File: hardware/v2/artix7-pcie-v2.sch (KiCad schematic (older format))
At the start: 0 parts

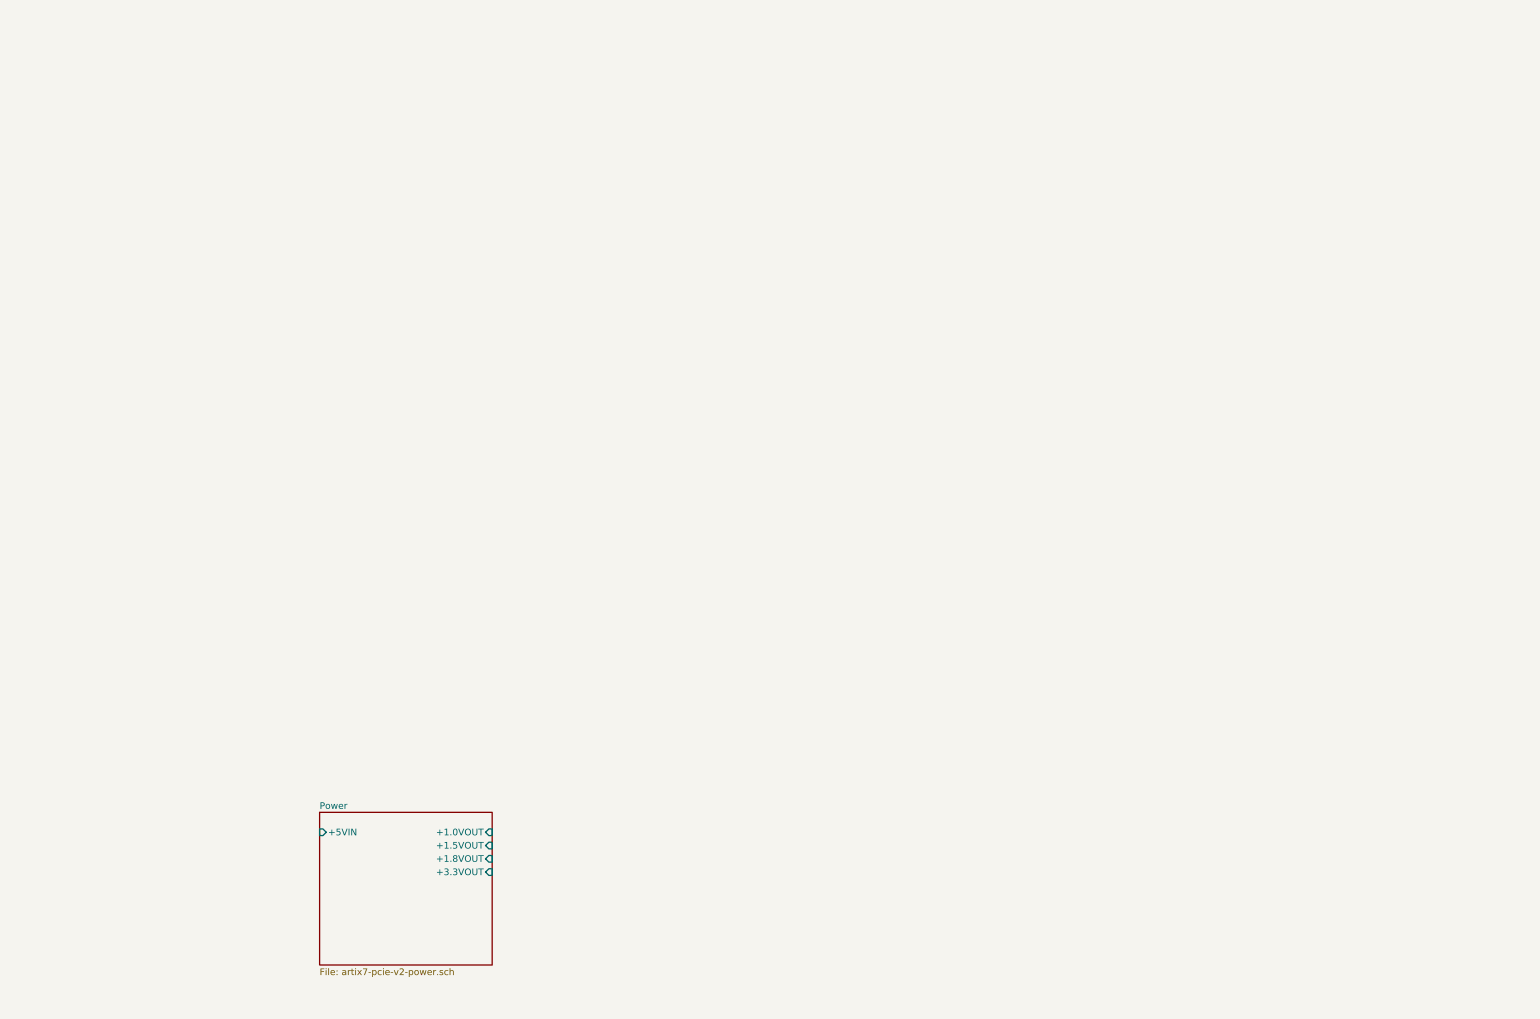
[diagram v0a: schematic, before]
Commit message: v2 schematic : add config block and connectors
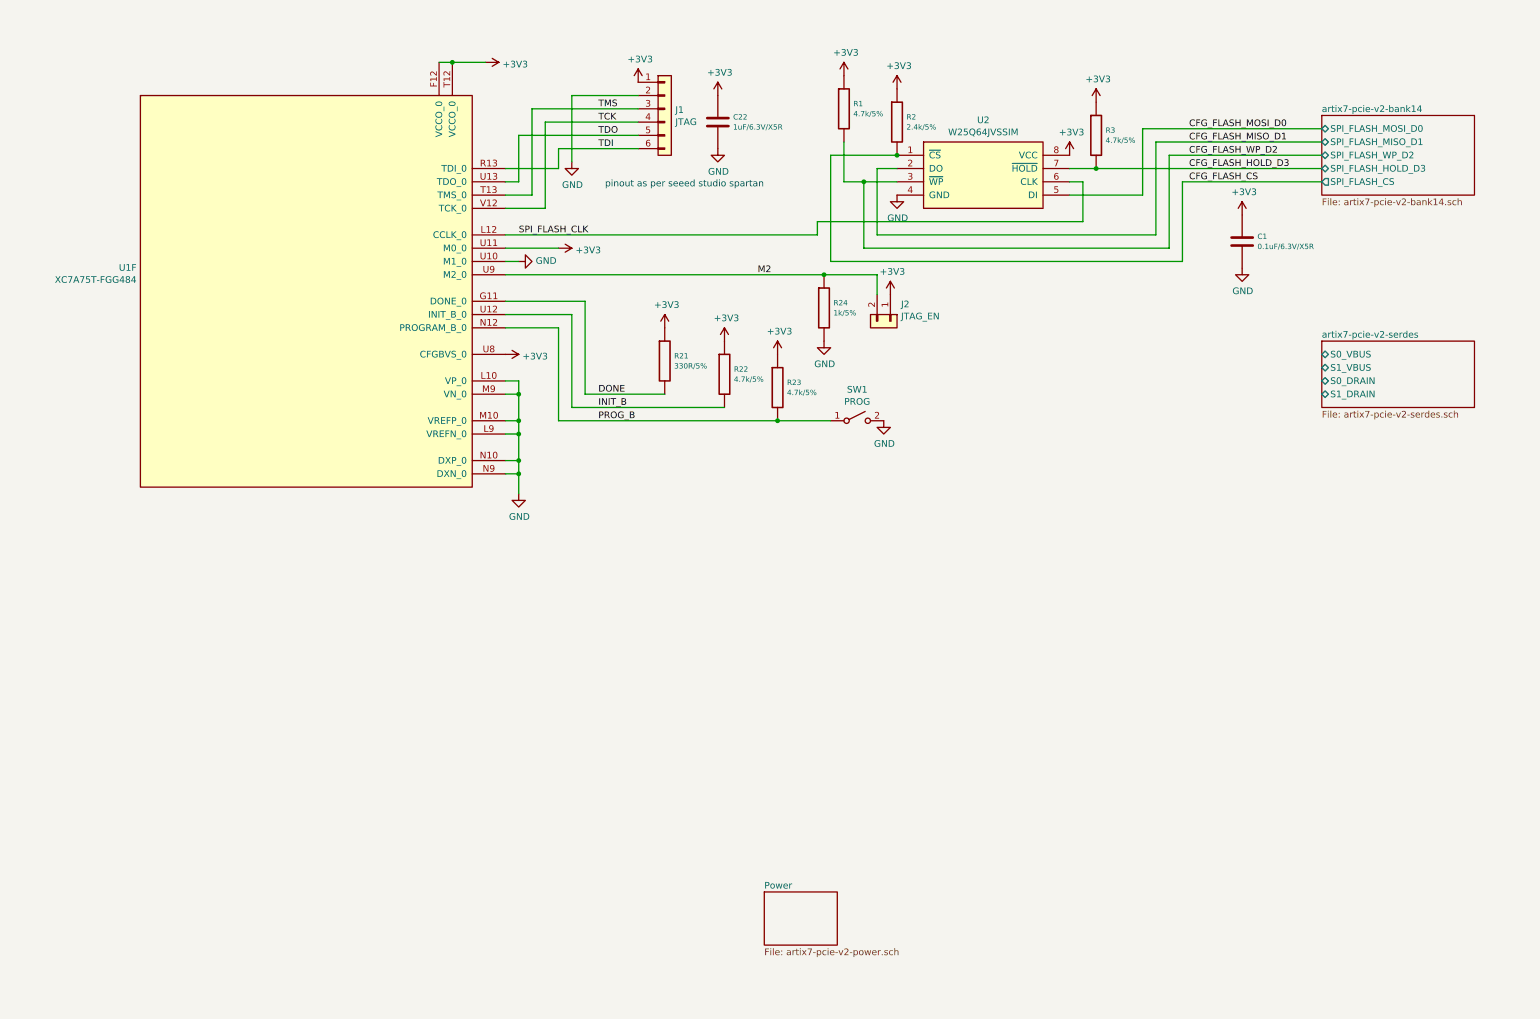
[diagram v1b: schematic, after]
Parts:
- added C1: 0.1uF/6.3V/X5R, tom-passives:C_0402_1005Metric, symbol tom-passives:C
- added C22: 1uF/6.3V/X5R, tom-passives:C_0402_1005Metric, symbol tom-passives:C
- added J1: JTAG, symbol tom-connectors:Conn_01x06
- added J2: JTAG_EN, symbol tom-connectors:Conn_01x02
- added R1, R22, R23, R3: 4.7k/5%, tom-passives:C_0402_1005Metric, symbol tom-passives:R
- added R2: 2.4k/5%, tom-passives:C_0402_1005Metric, symbol tom-passives:R
- added R21: 330R/5%, tom-passives:C_0402_1005Metric, symbol tom-passives:R
- added R24: 1k/5%, tom-passives:C_0402_1005Metric, symbol tom-passives:R
- added SW1: PROG, tom-mechanical:SW_Push_1P1T_NO_CK_KMR2, symbol tom-mechanical:SW_SPST
- added U1: XC7A75T-FGG484, artix7-pcie-v2:Xilinx_FGG484, symbol artix7-pcie-v2:XC7A75T-FGG484
- added U2: W25Q64JVSSIM, tom-semiconductors:SOIC-8_5.23x5.23mm_P1.27mm, symbol tom-semiconductors:W25Q128
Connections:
- new net +3V3: C1.1, C22.1, J1.1 (Pin_1), J2.1 (Pin_1), R1.1, R2.1, R21.1, R22.1, R23.1, R3.1, U1.F12 (VCCO_0), U1.T12 (VCCO_0), U1.U11 (M0_0), U1.U8 (CFGBVS_0), U2.8 (VCC)
- new net CFG_FLASH_CS: R2.2, U2.1 (~CS)
- new net CFG_FLASH_HOLD_D3: R3.2, U2.7 (~HOLD)
- new net CFG_FLASH_MISO_D1: U2.2 (DO)
- new net CFG_FLASH_MOSI_D0: U2.5 (DI)
- new net CFG_FLASH_WP_D2: R1.2, U2.3 (~WP)
- new net DONE: R21.2, U1.G11 (DONE_0)
- new net GND: C1.2, C22.2, J1.2 (Pin_2), R24.2, SW1.2 (B), U1.L10 (VP_0), U1.L9 (VREFN_0), U1.M10 (VREFP_0), U1.M9 (VN_0), U1.N10 (DXP_0), U1.N9 (DXN_0), U1.U10 (M1_0), U2.4 (GND)
- new net INIT_B: R22.2, U1.U12 (INIT_B_0)
- new net M2: J2.2 (Pin_2), R24.1, U1.U9 (M2_0)
- new net PROG_B: R23.2, SW1.1 (A), U1.N12 (PROGRAM_B_0)
- new net SPI_FLASH_CLK: U1.L12 (CCLK_0), U2.6 (CLK)
- new net TCK: J1.4 (Pin_4), U1.V12 (TCK_0)
- new net TDI: J1.6 (Pin_6), U1.R13 (TDI_0)
- new net TDO: J1.5 (Pin_5), U1.U13 (TDO_0)
- new net TMS: J1.3 (Pin_3), U1.T13 (TMS_0)
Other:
- note added: "pinout as per seeed studio spartan"

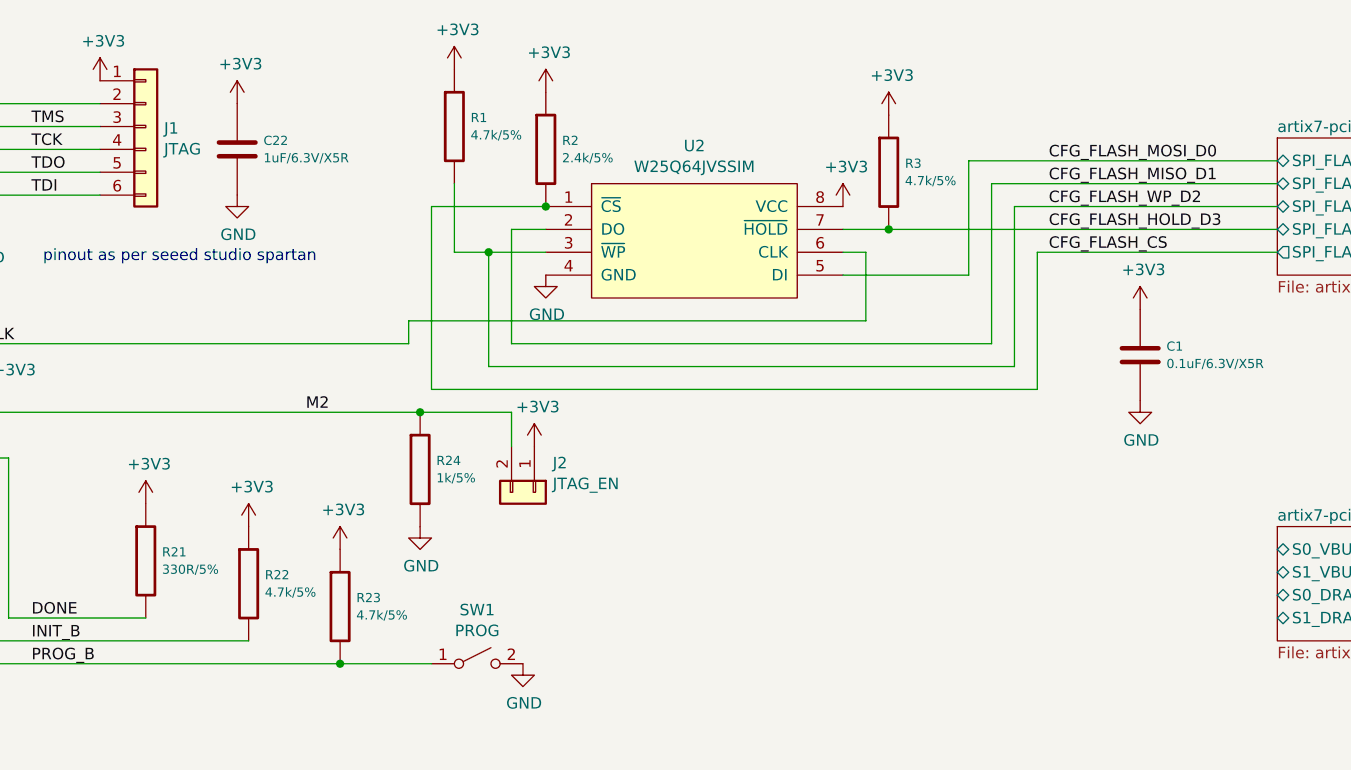
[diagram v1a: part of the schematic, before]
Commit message: v2 schematic: add bank14, serdes, fpga footprint
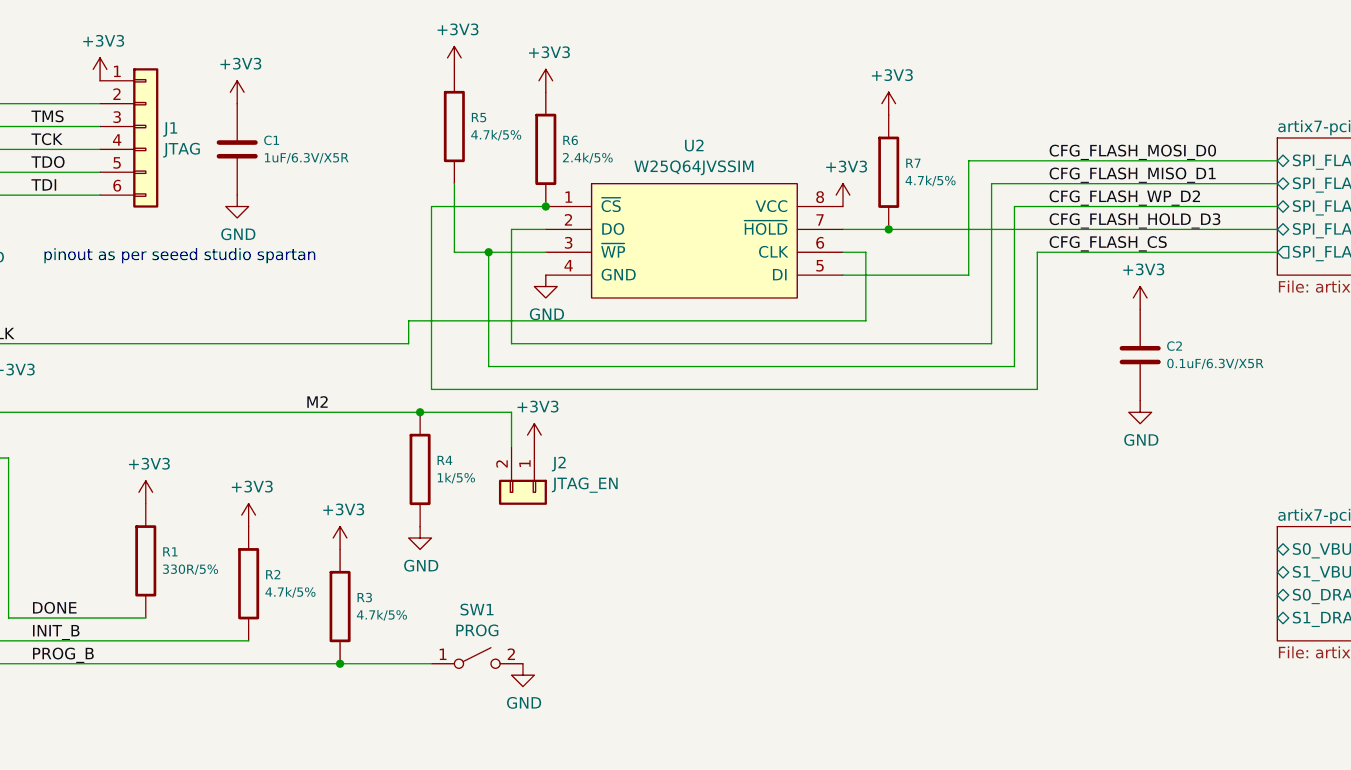
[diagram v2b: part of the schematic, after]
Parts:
- renumbered C22 to C1, C1 to C2, R21 to R1, R22 to R2, R23 to R3, R24 to R4, R1 to R5, R2 to R6, R3 to R7
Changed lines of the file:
@@
 $EndComp
 $Comp
-L tom-passives:C C1
+L tom-passives:C C2
 U 1 1 5E5AB0F3
 P 9200 1950
-F 0 "C1" H 9315 1988 40  0000 L CNN
+F 0 "C2" H 9315 1988 40  0000 L CNN
 F 1 "0.1uF/6.3V/X5R" H 9315 1912 40  0000 L CNN
 F 2 "tom-passives:C_0402_1005Metric" H 9238 1800 30  0001 C CNN
@@
 $EndComp
 $Comp
-L power:+3V3 #PWR06
+L power:+3V3 #PWR019
 U 1 1 5E5AC569
 P 7900 1300
-F 0 "#PWR06" H 7900 1150 50  0001 C CNN
+F 0 "#PWR019" H 7900 1150 50  0001 C CNN
 F 1 "+3V3" H 7915 1473 50  0000 C CNN
 F 2 "" H 7900 1300 50  0001 C CNN
@@
 $EndComp
 $Comp
-L power:+3V3 #PWR04
+L power:+3V3 #PWR021
 U 1 1 5E5ACB11
 P 9200 1750
-F 0 "#PWR04" H 9200 1600 50  0001 C CNN
+F 0 "#PWR021" H 9200 1600 50  0001 C CNN
 F 1 "+3V3" H 9215 1923 50  0000 C CNN
 F 2 "" H 9200 1750 50  0001 C CNN
@@
 $EndComp
 $Comp
-L power:GND #PWR05
+L power:GND #PWR022
 U 1 1 5E5AD9E3
 P 9200 2150
-F 0 "#PWR05" H 9200 1900 50  0001 C CNN
+F 0 "#PWR022" H 9200 1900 50  0001 C CNN
 F 1 "GND" H 9205 1977 50  0000 C CNN
 F 2 "" H 9200 2150 50  0001 C CNN
@@
 $EndComp
 $Comp
-L tom-passives:R R3
+L tom-passives:R R7
 U 1 1 5E5AE2B3
 P 8100 1150
-F 0 "R3" H 8171 1188 40  0000 L CNN
+F 0 "R7" H 8171 1188 40  0000 L CNN
 F 1 "4.7k/5%" H 8171 1112 40  0000 L CNN
 F 2 "tom-passives:C_0402_1005Metric" V 8030 1150 30  0001 C CNN
@@
 	7900 1400 8100 1400
 $Comp
-L tom-passives:R R2
+L tom-passives:R R6
 U 1 1 5E5AF5D9
 P 6600 1050
-F 0 "R2" H 6671 1088 40  0000 L CNN
+F 0 "R6" H 6671 1088 40  0000 L CNN
 F 1 "2.4k/5%" H 6671 1012 40  0000 L CNN
 F 2 "tom-passives:C_0402_1005Metric" V 6530 1050 30  0001 C CNN
@@
 	6200 1500 6350 1500
 $Comp
-L power:+3V3 #PWR07
+L power:+3V3 #PWR020
 U 1 1 5E5B03D8
 P 8100 900
-F 0 "#PWR07" H 8100 750 50  0001 C CNN
+F 0 "#PWR020" H 8100 750 50  0001 C CNN
 F 1 "+3V3" H 8115 1073 50  0000 C CNN
 F 2 "" H 8100 900 50  0001 C CNN
@@
 $EndComp
 $Comp
-L power:+3V3 #PWR02
+L power:+3V3 #PWR017
 U 1 1 5E5B073C
 P 6600 800
-F 0 "#PWR02" H 6600 650 50  0001 C CNN
+F 0 "#PWR017" H 6600 650 50  0001 C CNN
 F 1 "+3V3" H 6615 973 50  0000 C CNN
 F 2 "" H 6600 800 50  0001 C CNN
@@
 $EndComp
 $Comp
-L power:+3V3 #PWR01
+L power:+3V3 #PWR014
 U 1 1 5E5B0A8B
 P 6200 700
-F 0 "#PWR01" H 6200 550 50  0001 C CNN
+F 0 "#PWR014" H 6200 550 50  0001 C CNN
 F 1 "+3V3" H 6215 873 50  0000 C CNN
 F 2 "" H 6200 700 50  0001 C CNN
@@
 $EndComp
 $Comp
-L tom-passives:R R1
+L tom-passives:R R5
 U 1 1 5E5AFC9F
 P 6200 950
-F 0 "R1" H 6271 988 40  0000 L CNN
+F 0 "R5" H 6271 988 40  0000 L CNN
 F 1 "4.7k/5%" H 6271 912 40  0000 L CNN
 F 2 "tom-passives:C_0402_1005Metric" V 6130 950 30  0001 C CNN
@@
 CFG_FLASH_WP_D2
 $Comp
-L power:GND #PWR03
+L power:GND #PWR018
 U 1 1 5E5BCAAF
 P 6600 1600
-F 0 "#PWR03" H 6600 1350 50  0001 C CNN
+F 0 "#PWR018" H 6600 1350 50  0001 C CNN
 F 1 "GND" H 6605 1427 50  0000 C CNN
 F 2 "" H 6600 1600 50  0001 C CNN
@@
 $EndComp
 $Comp
-L power:+3V3 #PWR0101
+L power:+3V3 #PWR07
 U 1 1 5E6BF0FA
 P 4650 750
-F 0 "#PWR0101" H 4650 600 50  0001 C CNN
+F 0 "#PWR07" H 4650 600 50  0001 C CNN
 F 1 "+3V3" H 4665 923 50  0000 C CNN
 F 2 "" H 4650 750 50  0001 C CNN
@@
 	4150 850  4150 1350
 $Comp
-L power:GND #PWR0102
+L power:GND #PWR06
 U 1 1 5E6D5933
 P 4150 1350
-F 0 "#PWR0102" H 4150 1100 50  0001 C CNN
+F 0 "#PWR06" H 4150 1100 50  0001 C CNN
 F 1 "GND" H 4155 1177 50  0000 C CNN
 F 2 "" H 4150 1350 50  0001 C CNN
@@
 TDI
 $Comp
-L tom-passives:C C22
+L tom-passives:C C1
 U 1 1 5E743267
 P 5250 1050
-F 0 "C22" H 5365 1088 40  0000 L CNN
+F 0 "C1" H 5365 1088 40  0000 L CNN
 F 1 "1uF/6.3V/X5R" H 5365 1012 40  0000 L CNN
 F 2 "tom-passives:C_0402_1005Metric" H 5288 900 30  0001 C CNN
@@
 $EndComp
 $Comp
-L power:+3V3 #PWR0103
+L power:+3V3 #PWR09
 U 1 1 5E743271
 P 5250 850
-F 0 "#PWR0103" H 5250 700 50  0001 C CNN
+F 0 "#PWR09" H 5250 700 50  0001 C CNN
 F 1 "+3V3" H 5265 1023 50  0000 C CNN
 F 2 "" H 5250 850 50  0001 C CNN
@@
 $EndComp
 $Comp
-L power:GND #PWR0104
+L power:GND #PWR010
 U 1 1 5E74327B
 P 5250 1250
-F 0 "#PWR0104" H 5250 1000 50  0001 C CNN
+F 0 "#PWR010" H 5250 1000 50  0001 C CNN
 F 1 "GND" H 5255 1077 50  0000 C CNN
 F 2 "" H 5250 1250 50  0001 C CNN
@@
 pinout as per seeed studio spartan
 $Comp
-L tom-passives:R R23
+L tom-passives:R R3
 U 1 1 5E75FBB7
 P 5700 3050
-F 0 "R23" H 5771 3088 40  0000 L CNN
+F 0 "R3" H 5771 3088 40  0000 L CNN
 F 1 "4.7k/5%" H 5771 3012 40  0000 L CNN
 F 2 "tom-passives:C_0402_1005Metric" V 5630 3050 30  0001 C CNN
@@
 $EndComp
 $Comp
-L tom-passives:R R22
+L tom-passives:R R2
 U 1 1 5E760C75
 P 5300 2950
-F 0 "R22" H 5371 2988 40  0000 L CNN
+F 0 "R2" H 5371 2988 40  0000 L CNN
 F 1 "4.7k/5%" H 5371 2912 40  0000 L CNN
 F 2 "tom-passives:C_0402_1005Metric" V 5230 2950 30  0001 C CNN
@@
 $EndComp
 $Comp
-L power:+3V3 #PWR0105
+L power:+3V3 #PWR011
 U 1 1 5E7753ED
 P 5300 2700
-F 0 "#PWR0105" H 5300 2550 50  0001 C CNN
+F 0 "#PWR011" H 5300 2550 50  0001 C CNN
 F 1 "+3V3" H 5315 2873 50  0000 C CNN
 F 2 "" H 5300 2700 50  0001 C CNN
@@
 $EndComp
 $Comp
-L power:+3V3 #PWR0106
+L power:+3V3 #PWR012
 U 1 1 5E77616B
 P 5700 2800
-F 0 "#PWR0106" H 5700 2650 50  0001 C CNN
+F 0 "#PWR012" H 5700 2650 50  0001 C CNN
 F 1 "+3V3" H 5715 2973 50  0000 C CNN
 F 2 "" H 5700 2800 50  0001 C CNN
@@
 	4250 3100 4850 3100
 $Comp
-L tom-passives:R R21
+L tom-passives:R R1
 U 1 1 5E7A8CB7
 P 4850 2850
-F 0 "R21" H 4921 2888 40  0000 L CNN
+F 0 "R1" H 4921 2888 40  0000 L CNN
 F 1 "330R/5%" H 4921 2812 40  0000 L CNN
 F 2 "tom-passives:C_0402_1005Metric" V 4780 2850 30  0001 C CNN
@@
 $EndComp
 $Comp
-L power:+3V3 #PWR0107
+L power:+3V3 #PWR08
 U 1 1 5E7AB876
 P 4850 2600
-F 0 "#PWR0107" H 4850 2450 50  0001 C CNN
+F 0 "#PWR08" H 4850 2450 50  0001 C CNN
 F 1 "+3V3" H 4865 2773 50  0000 C CNN
 F 2 "" H 4850 2600 50  0001 C CNN
@@
 DONE
 $Comp
-L power:+3V3 #PWR0108
+L power:+3V3 #PWR02
 U 1 1 5E7BD9F2
 P 3650 2800
-F 0 "#PWR0108" H 3650 2650 50  0001 C CNN
+F 0 "#PWR02" H 3650 2650 50  0001 C CNN
 F 1 "+3V3" V 3665 2928 50  0000 L CNN
 F 2 "" H 3650 2800 50  0001 C CNN
@@
 	3750 3000 3750 3100
 $Comp
-L power:GND #PWR0109
+L power:GND #PWR04
 U 1 1 5E7C01C5
 P 3750 3850
-F 0 "#PWR0109" H 3750 3600 50  0001 C CNN
+F 0 "#PWR04" H 3750 3600 50  0001 C CNN
 F 1 "GND" H 3755 3677 50  0000 C CNN
 F 2 "" H 3750 3850 50  0001 C CNN
@@
 	3650 2100 3750 2100
 $Comp
-L power:GND #PWR0110
+L power:GND #PWR03
 U 1 1 5E7EE2B7
 P 3750 2100
-F 0 "#PWR0110" H 3750 1850 50  0001 C CNN
+F 0 "#PWR03" H 3750 1850 50  0001 C CNN
 F 1 "GND" V 3755 1972 50  0000 R CNN
 F 2 "" H 3750 2100 50  0001 C CNN
@@
 $EndComp
 $Comp
-L tom-passives:R R24
+L tom-passives:R R4
 U 1 1 5E7FB45A
 P 6050 2450
-F 0 "R24" H 6121 2488 40  0000 L CNN
+F 0 "R4" H 6121 2488 40  0000 L CNN
 F 1 "1k/5%" H 6121 2412 40  0000 L CNN
 F 2 "tom-passives:C_0402_1005Metric" V 5980 2450 30  0001 C CNN
@@
 $EndComp
 $Comp
-L power:GND #PWR0111
+L power:GND #PWR013
 U 1 1 5E7FCD8A
 P 6050 2700
-F 0 "#PWR0111" H 6050 2450 50  0001 C CNN
+F 0 "#PWR013" H 6050 2450 50  0001 C CNN
 F 1 "GND" H 6055 2527 50  0000 C CNN
 F 2 "" H 6050 2700 50  0001 C CNN
@@
 $EndComp
 $Comp
-L power:+3V3 #PWR0112
+L power:+3V3 #PWR05
 U 1 1 5E815253
 P 4050 2000
-F 0 "#PWR0112" H 4050 1850 50  0001 C CNN
+F 0 "#PWR05" H 4050 1850 50  0001 C CNN
 F 1 "+3V3" V 4065 2128 50  0000 L CNN
 F 2 "" H 4050 2000 50  0001 C CNN
@@
 Connection ~ 6050 2200
 $Comp
-L power:+3V3 #PWR0113
+L power:+3V3 #PWR016
 U 1 1 5E82C135
 P 6550 2350
-F 0 "#PWR0113" H 6550 2200 50  0001 C CNN
+F 0 "#PWR016" H 6550 2200 50  0001 C CNN
 F 1 "+3V3" H 6565 2523 50  0000 C CNN
 F 2 "" H 6550 2350 50  0001 C CNN
@@
 Connection ~ 5700 3300
 $Comp
-L power:GND #PWR0114
+L power:GND #PWR015
 U 1 1 5E83C7AF
 P 6500 3300
-F 0 "#PWR0114" H 6500 3050 50  0001 C CNN
+F 0 "#PWR015" H 6500 3050 50  0001 C CNN
 F 1 "GND" H 6505 3127 50  0000 C CNN
 F 2 "" H 6500 3300 50  0001 C CNN
@@
 	3650 2200 6050 2200
 $Comp
-L power:+3V3 #PWR0115
+L power:+3V3 #PWR01
 U 1 1 5E95EFB5
 P 3500 600
-F 0 "#PWR0115" H 3500 450 50  0001 C CNN
+F 0 "#PWR01" H 3500 450 50  0001 C CNN
 F 1 "+3V3" V 3515 728 50  0000 L CNN
 F 2 "" H 3500 600 50  0001 C CNN
